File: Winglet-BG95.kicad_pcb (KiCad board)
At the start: 4 copper layers, 30 x 47.6 mm, 43 parts, among them J1 2337019-1, J2 2337019-1, J3 1042240820, M1 PTH_M2.5, M2 PTH_M2.5, Q1 DMG1012UW-7, Q2 DMG1012UW-7, U1 BG95MxLA, U2 MFF2-SIM, U3 24AA01T-I/OT, U4 FXLA108BQX

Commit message: Nitpicks before release
Update output scripts
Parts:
- moved TP1 0.10 mm to (65.4, 69.9)
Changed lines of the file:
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@@
 			(layer "F.Mask"
 				(type "Top Solder Mask")
-				(color "Blue")
+				(color "Black")
 				(thickness 0.01)
 			)
@@
 			(layer "B.Mask"
 				(type "Bottom Solder Mask")
-				(color "Blue")
+				(color "Black")
 				(thickness 0.01)
 			)
@@
 		(at 75.2 63.8 180)
 		(property "Reference" "R1"
-			(at -2.05 0 0)
+			(at -2.25 0 0)
 			(layer "F.SilkS")
 			(effects
@@
 		(at 57.05 93.735 90)
 		(property "Reference" "U4"
-			(at -2.365 -0.15 0)
+			(at -2.115 0.05 180)
 			(layer "F.SilkS")
 			(effects
@@
 			(layer "F.Fab")
 		)
+		(fp_text user "${REFERENCE}"
+			(at 0 0 180)
+			(layer "F.Fab")
+			(effects
+				(font
+					(size 0.75 0.75)
+					(thickness 0.11)
+				)
+			)
+		)
 		(pad "1" smd oval
 			(at -0.25 -2.135)
@@
 		(at 60.345 84.7 -90)
 		(property "Reference" "C13"
-			(at 0.05 1.4 90)
+			(at 0.05 1.295 90)
 			(layer "F.SilkS")
 			(effects
@@
 		(at 52.8 94.6 180)
 		(property "Reference" "C15"
-			(at 0.145 -1.25 0)
+			(at 0.1 -1.35 0)
 			(layer "F.SilkS")
 			(effects
@@
 		(at 63.895 86.65 90)
 		(property "Reference" "U2"
-			(at 4 -0.045 180)
+			(at 3.95 0.005 180)
 			(layer "F.SilkS")
 			(effects
@@
 			(layer "F.Fab")
 		)
+		(fp_text user "${REFERENCE}"
+			(at 0 0 90)
+			(unlocked yes)
+			(layer "F.Fab")
+			(effects
+				(font
+					(size 1 1)
+					(thickness 0.15)
+				)
+			)
+		)
 		(pad "" smd roundrect
 			(at -0.8 -0.9 90)
@@
 		(at 52.775 93.1 180)
 		(property "Reference" "C16"
-			(at 0 1.3 0)
+			(at 0.025 1.3 0)
 			(layer "F.SilkS")
 			(effects
@@
 	(footprint "TP_TestPoint:TestPoint_1mm"
 		(layer "B.Cu")
-		(at 65.3 69.9 180)
+		(at 65.4 69.9 180)
 		(descr "SMD pad as test Point, diameter 1.0mm")
 		(tags "test point SMD pad")
@@
 			(effects
 				(font
-					(size 0.8 0.8)
+					(size 1 1)
 					(thickness 0.15)
 				)
@@
 			(end 0 -0.7)
 			(stroke
-				(width 0.12)
+				(width 0.15)
 				(type solid)
 			)
@@
 			(layer "B.CrtYd")
 		)
+		(fp_circle
+			(center 0 0)
+			(end 0.7 0)
+			(stroke
+				(width 0.1)
+				(type default)
+			)
+			(fill no)
+			(layer "B.Fab")
+		)
 		(fp_text user "${REFERENCE}"

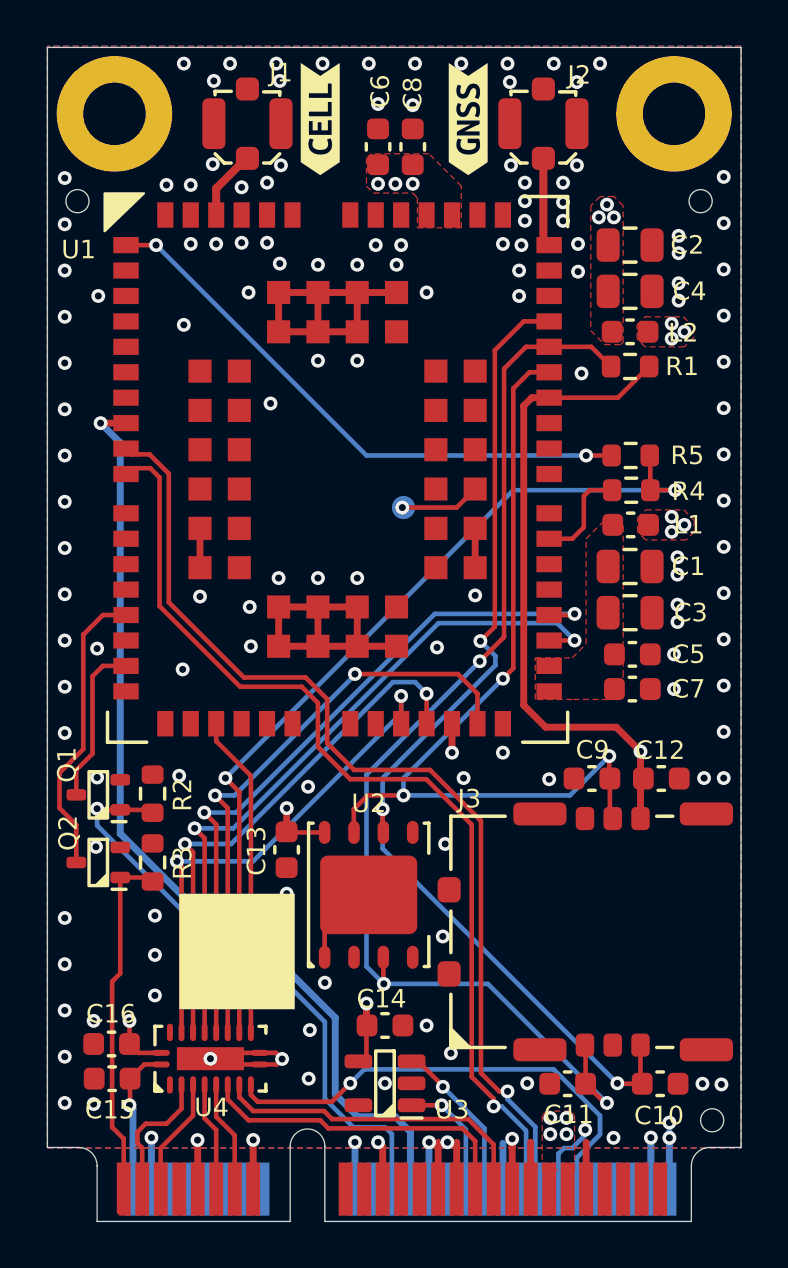
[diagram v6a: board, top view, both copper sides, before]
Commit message: Move to NSIM-16-B sim card holder for easier sourcing
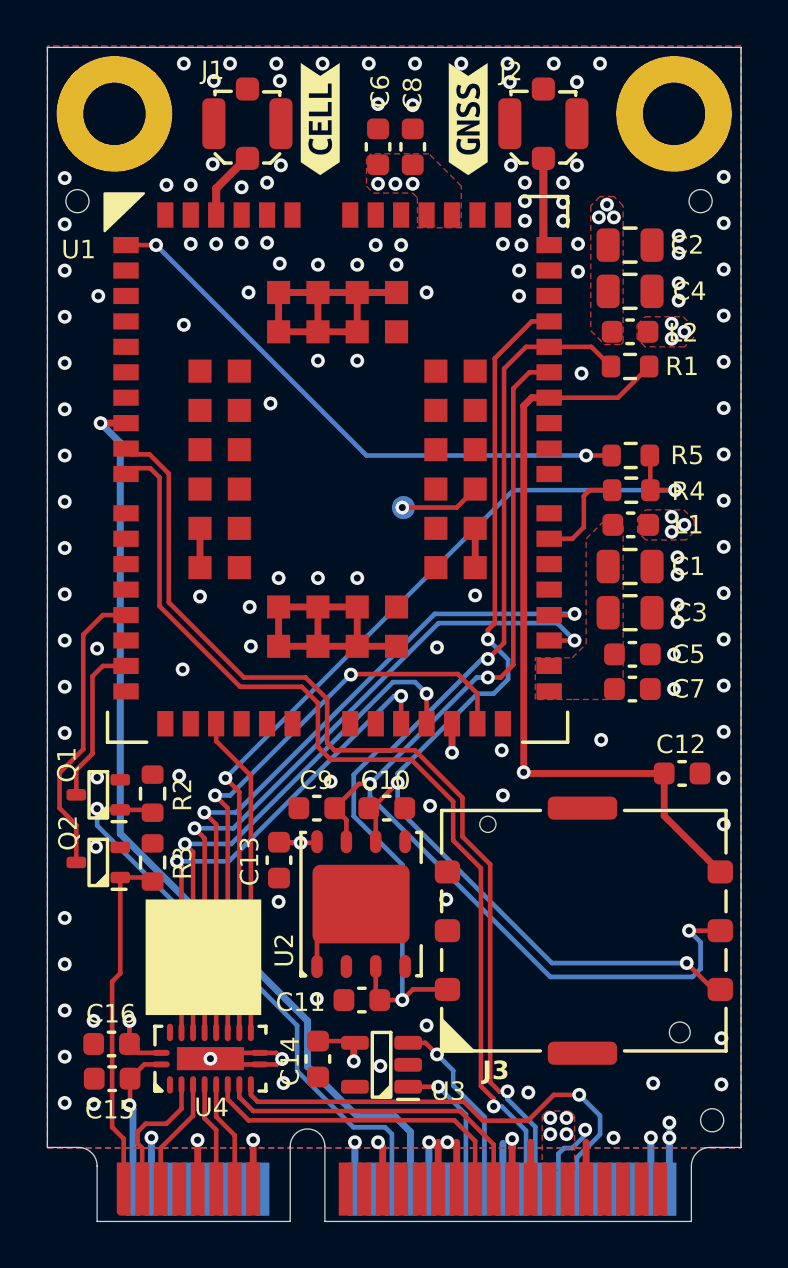
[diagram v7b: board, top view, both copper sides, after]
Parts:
- J1, J2: footprint J_Connector:A-1JB -> J_Connector:U.FL
- J3: value 1042240820 -> NSIM-16-B; footprint J_Connector:1042240820 -> J_Connector:NSIM-16-B
- R2, R3: value 100K -> 10K
- U1: value BG95MxLA -> BG95M1LA
- moved C10 16.8 mm to (64.7, 82.9)
- moved C9 12.0 mm to (61.6, 82.9)
- moved C11 9.61 mm to (63.6, 91.2)
- moved C14 3.24 mm to (61.7, 93.8), turned to -90 degrees
- moved N1 1.47 mm to (56.8, 89.3)
- moved C12 0.93 mm to (77.5, 81.4)
- moved U3 0.81 mm to (64.5, 94.0)
- moved C13 0.56 mm to (60.0, 85.2)
- moved U2 0.52 mm to (63.6, 87.0)
- moved J3 0.12 mm to (73.1, 88.2)
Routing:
- net /Memory/USIM_RST: track 37.4 -> 47.2 mm
- net /Memory/USIM_DATA: track 50.6 -> 41.7 mm, vias 3 -> 2
- net +VDDIO: track 22.0 -> 19.4 mm
- net /Connector/I2C_SDA: track 7.00 -> 8.13 mm
- net /Memory/USIM_VDD: track 47.5 -> 46.7 mm
- net /Connector/RESET: track 25.8 -> 25.0 mm
- net /Connector/USB_VBUS: track 41.5 -> 40.7 mm
- net GND: track 71.1 -> 70.4 mm, vias 145 -> 143
- net /Connector/I2C_SCL: track 5.36 -> 6.07 mm
